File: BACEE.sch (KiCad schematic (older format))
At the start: 13 parts, among them U1 DS1337_PDv2, U2 24LC1025, U3 24LC1025, U4 ATMEGA328P-AU, Y1 Crystal, Y2 Crystal

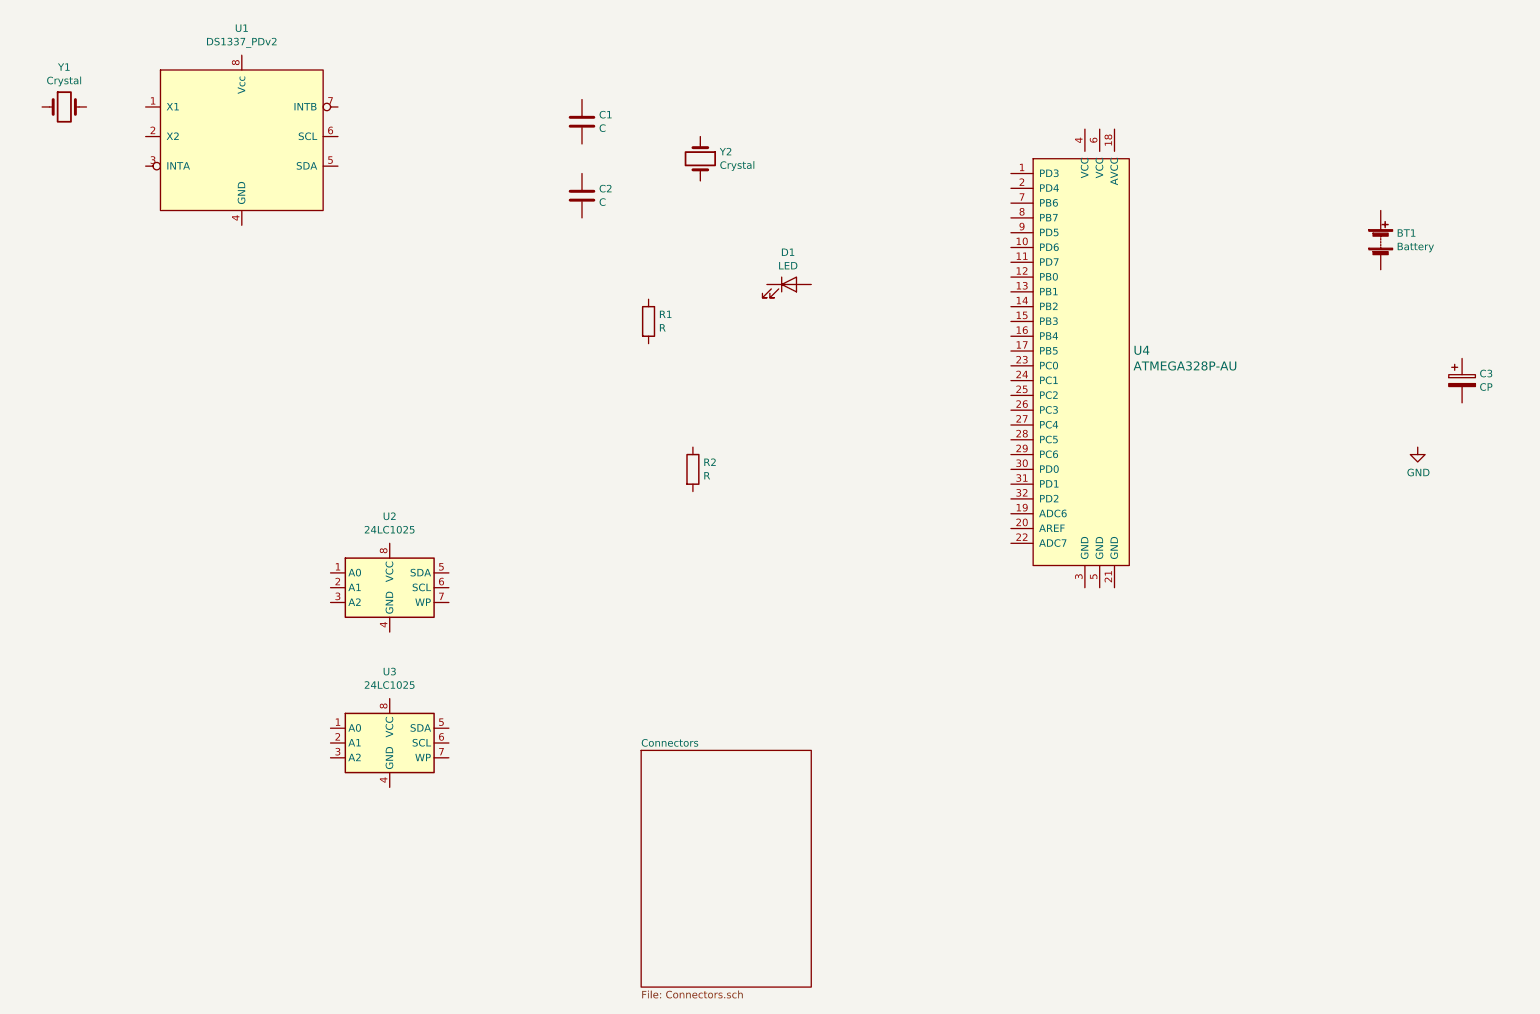
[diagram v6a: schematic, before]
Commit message: Completed wiring in connector sheet
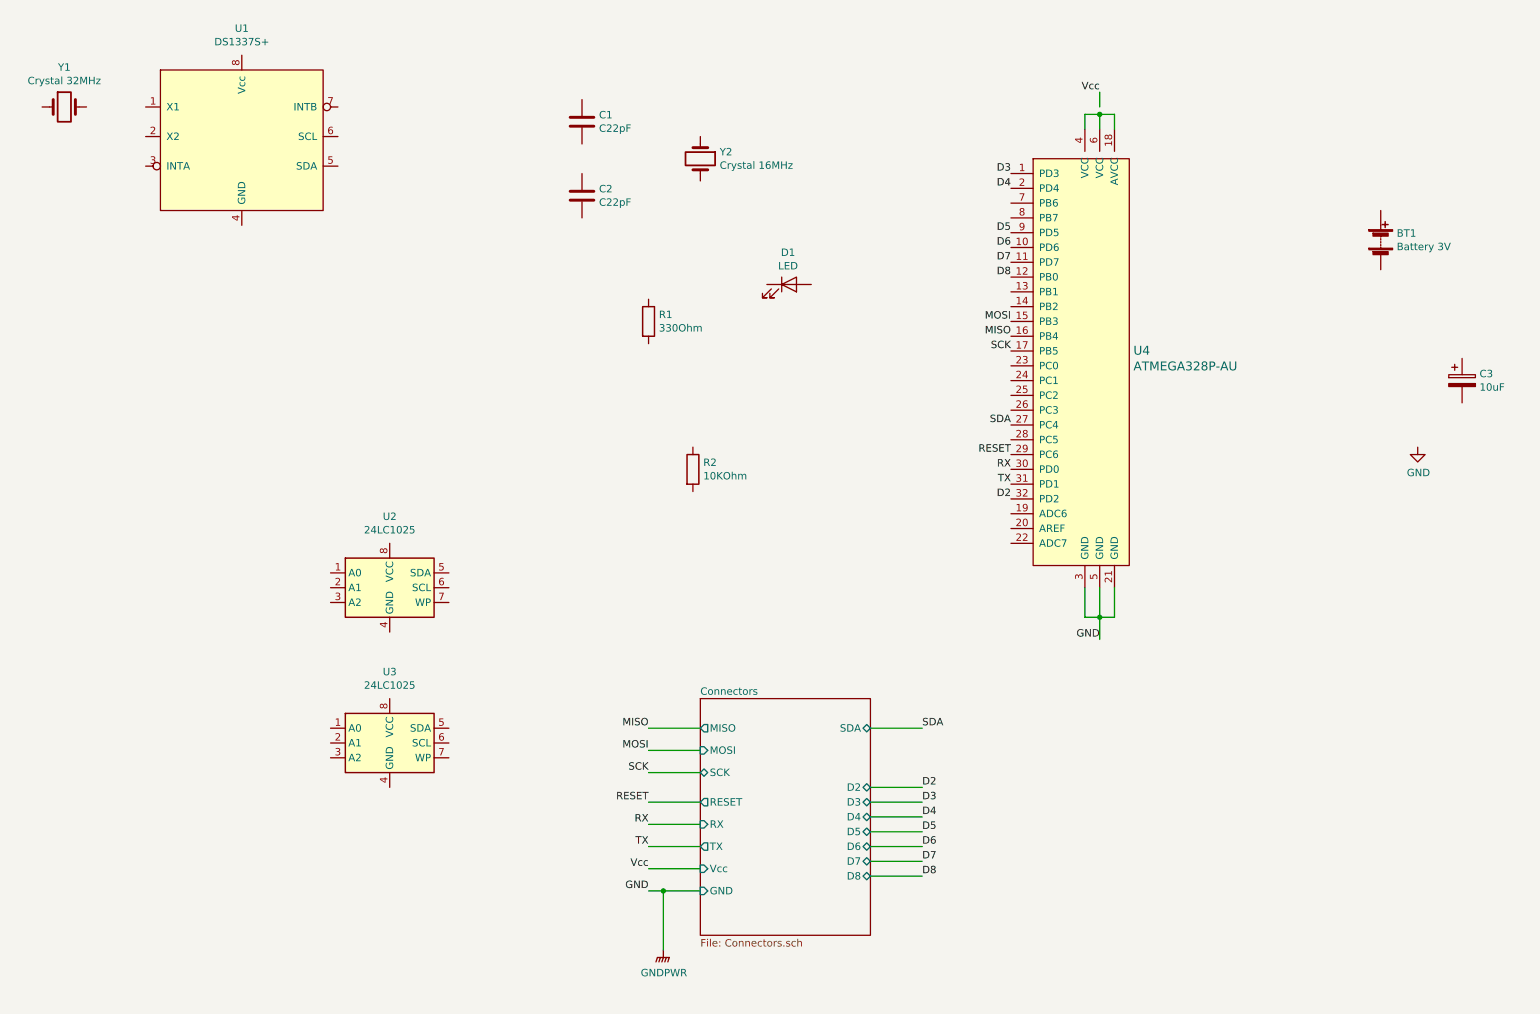
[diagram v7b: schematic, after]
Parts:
- BT1: value Battery -> Battery 3V
- C1, C2: value C -> C22pF
- C3: value CP -> 10uF
- R1: value R -> 330Ohm
- R2: value R -> 10KOhm
- U1: value DS1337_PDv2 -> DS1337S+
- Y1: value Crystal -> Crystal 32MHz
- Y2: value Crystal -> Crystal 16MHz
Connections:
- net labels added: D2, D3, D4, D5, D6, D7, D8, GNDPWR, MISO, MOSI, RESET, RX, SCK, SDA, TX, Vcc
- wire segments 0 -> 30
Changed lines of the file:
@@
 P 9800 2600
 F 0 "BT1" H 9908 2646 50  0000 L CNN
-F 1 "Battery" H 9908 2555 50  0000 L CNN
+F 1 "Battery 3V" H 9908 2555 50  0000 L CNN
 F 2 "Connector_PinHeader_2.54mm:PinHeader_1x02_P2.54mm_Vertical" V 9800 2660 50  0001 C CNN
 F 3 "~" V 9800 2660 50  0001 C CNN
@@
 P 4400 1800
 F 0 "C1" H 4515 1846 50  0000 L CNN
-F 1 "C" H 4515 1755 50  0000 L CNN
+F 1 "C22pF" H 4515 1755 50  0000 L CNN
 F 2 "Capacitor_SMD:C_0805_2012Metric_Pad1.15x1.40mm_HandSolder" H 4438 1650 50  0001 C CNN
 F 3 "~" H 4400 1800 50  0001 C CNN
@@
 P 4400 2300
 F 0 "C2" H 4515 2346 50  0000 L CNN
-F 1 "C" H 4515 2255 50  0000 L CNN
+F 1 "C22pF" H 4515 2255 50  0000 L CNN
 F 2 "Capacitor_SMD:C_0805_2012Metric_Pad1.15x1.40mm_HandSolder" H 4438 2150 50  0001 C CNN
 F 3 "~" H 4400 2300 50  0001 C CNN
@@
 P 10350 3550
 F 0 "C3" H 10468 3596 50  0000 L CNN
-F 1 "CP" H 10468 3505 50  0000 L CNN
+F 1 "10uF" H 10468 3505 50  0000 L CNN
 F 2 "Capacitor_SMD:C_0805_2012Metric_Pad1.15x1.40mm_HandSolder" H 10388 3400 50  0001 C CNN
 F 3 "~" H 10350 3550 50  0001 C CNN
@@
 P 4850 3150
 F 0 "R1" H 4920 3196 50  0000 L CNN
-F 1 "R" H 4920 3105 50  0000 L CNN
+F 1 "330Ohm" H 4920 3105 50  0000 L CNN
 F 2 "Resistor_SMD:R_0805_2012Metric_Pad1.15x1.40mm_HandSolder" V 4780 3150 50  0001 C CNN
 F 3 "~" H 4850 3150 50  0001 C CNN
@@
 P 5150 4150
 F 0 "R2" H 5220 4196 50  0000 L CNN
-F 1 "R" H 5220 4105 50  0000 L CNN
+F 1 "10KOhm" H 5220 4105 50  0000 L CNN
 F 2 "Resistor_SMD:R_0805_2012Metric_Pad1.15x1.40mm_HandSolder" V 5080 4150 50  0001 C CNN
 F 3 "~" H 5150 4150 50  0001 C CNN
@@
 $EndComp
 $Sheet
-S 4800 6050 1150 1600
+S 5200 5700 1150 1600
 U 5EC178C4
 F0 "Connectors" 50
 F1 "Connectors.sch" 50
+F2 "MISO" O L 5200 5900 50
+F3 "SCK" B L 5200 6200 50
+F4 "RESET" O L 5200 6400 50
+F5 "Vcc" I L 5200 6850 50
+F6 "MOSI" I L 5200 6050 50
+F7 "GND" I L 5200 7000 50
+F8 "RX" I L 5200 6550 50
+F9 "TX" O L 5200 6700 50
+F10 "SDA" B R 6350 5900 50
+F11 "D2" B R 6350 6300 50
+F12 "D3" B R 6350 6400 50
+F13 "D4" B R 6350 6500 50
+F14 "D5" B R 6350 6600 50
+F15 "D6" B R 6350 6700 50
+F16 "D8" B R 6350 6900 50
+F17 "D7" B R 6350 6800 50
 $EndSheet
 $Comp
@@
 P 2100 1900
 F 0 "U1" H 2100 2631 50  0000 C CNN
-F 1 "DS1337_PDv2" H 2100 2540 50  0000 C CNN
+F 1 "DS1337S+" H 2100 2540 50  0000 C CNN
 F 2 "Package_SO:SOIJ-8_5.3x5.3mm_P1.27mm" H 3050 2400 50  0001 C CNN
 F 3 "https://4donline.ihs.com/images/VipMasterIC/IC/MAXM/MAXM-S-A0000633411/MAXM-S-A0000771822-1.pdf?hkey=52A5661711E402568146F3353EA87419" H 3050 2400 50  0001 C CNN
@@
 P 900 1700
 F 0 "Y1" H 900 1968 50  0000 C CNN
-F 1 "Crystal" H 900 1877 50  0000 C CNN
+F 1 "Crystal 32MHz" H 900 1877 50  0000 C CNN
 F 2 "Crystal:Crystal_SMD_MicroCrystal_CC7V-T1A-2Pin_3.2x1.5mm" H 900 1700 50  0001 C CNN
 F 3 "~" H 900 1700 50  0001 C CNN
@@
 P 5200 2050
 F 0 "Y2" V 5154 2181 50  0000 L CNN
-F 1 "Crystal" V 5245 2181 50  0000 L CNN
+F 1 "Crystal 16MHz" V 5245 2181 50  0000 L CNN
 F 2 "Crystal:Crystal_SMD_5032-2Pin_5.0x3.2mm_HandSoldering" H 5200 2050 50  0001 C CNN
 F 3 "~" H 5200 2050 50  0001 C CNN
@@
 	1    0    0    -1
 $EndComp
+Text Label 4850 5900 2    50   ~ 0
+MISO
+Wire Wire Line
+	4850 5900 5200 5900
+Text Label 7300 3250 2    50   ~ 0
+MISO
+Text Label 4850 6200 2    50   ~ 0
+SCK
+Text Label 4850 6400 2    50   ~ 0
+RESET
+Text Label 4850 6850 2    50   ~ 0
+Vcc
+Text Label 4850 6050 2    50   ~ 0
+MOSI
+Text Label 4850 7000 2    50   ~ 0
+GND
+Wire Wire Line
+	5200 6200 4850 6200
+Wire Wire Line
+	5200 6400 4850 6400
+Wire Wire Line
+	5200 6850 4850 6850
+Wire Wire Line
+	5200 6050 4850 6050
+Wire Wire Line
+	5200 7000 4950 7000
+Text Label 7300 3150 2    50   ~ 0
+MOSI
+Text Label 7300 3350 2    50   ~ 0
+SCK
+Text Label 7300 4050 2    50   ~ 0
+RESET
+Text Label 7900 1600 2    50   ~ 0
+Vcc
+Wire Wire Line
+	7800 1850 7800 1750
+Wire Wire Line
+	7800 1750 7900 1750
+Wire Wire Line
+	8000 1750 8000 1850
+Wire Wire Line
+	7900 1850 7900 1750
+Connection ~ 7900 1750
+Wire Wire Line
+	7900 1750 8000 1750
+Wire Wire Line
+	7900 1700 7900 1600
+Text Label 7900 5300 2    50   ~ 0
+GND
+Wire Wire Line
+	8000 5150 8000 4950
+Wire Wire Line
+	7900 4950 7900 5150
+Wire Wire Line
+	7900 5150 8000 5150
+Wire Wire Line
+	7800 5150 7900 5150
+Connection ~ 7900 5150
+Wire Wire Line
+	7800 4950 7800 5150
+Wire Wire Line
+	7900 5150 7900 5300
+$Comp
+L power:GNDPWR #PWR?
+U 1 1 5EC52C1A
+P 4950 7400
+F 0 "#PWR?" H 4950 7200 50  0001 C CNN
+F 1 "GNDPWR" H 4954 7246 50  0000 C CNN
+F 2 "" H 4950 7350 50  0001 C CNN
+F 3 "" H 4950 7350 50  0001 C CNN
+	1    4950 7400
+	1    0    0    -1
+$EndComp
+Wire Wire Line
+	4950 7400 4950 7000
+Connection ~ 4950 7000
+Wire Wire Line
+	4950 7000 4850 7000
+Text Label 6700 5900 0    50   ~ 0
+SDA
+Text Label 6700 6300 0    50   ~ 0
+D2
+Text Label 6700 6400 0    50   ~ 0
+D3
+Text Label 6700 6500 0    50   ~ 0
+D4
+Text Label 6700 6600 0    50   ~ 0
+D5
+Text Label 6700 6700 0    50   ~ 0
+D6
+Text Label 6700 6800 0    50   ~ 0
+D7
+Text Label 6700 6900 0    50   ~ 0
+D8
+Text Label 4850 6550 2    50   ~ 0
+RX
+Text Label 4850 6700 2    50   ~ 0
+TX
+Wire Wire Line
+	6350 5900 6700 5900
+Wire Wire Line
+	6350 6300 6700 6300
+Wire Wire Line
+	6700 6400 6350 6400
+Wire Wire Line
+	6350 6500 6700 6500
+Wire Wire Line
+	6700 6600 6350 6600
+Wire Wire Line
+	6350 6700 6700 6700
+Wire Wire Line
+	6700 6800 6350 6800
+Wire Wire Line
+	6350 6900 6700 6900
+Wire Wire Line
+	5200 6700 4850 6700
+Wire Wire Line
+	5200 6550 4850 6550
+Text Label 7300 2150 2    50   ~ 0
+D3
+Text Label 7300 2250 2    50   ~ 0
+D4
+Text Label 7300 2550 2    50   ~ 0
+D5
+Text Label 7300 2650 2    50   ~ 0
+D6
+Text Label 7300 2750 2    50   ~ 0
+D7
+Text Label 7300 2850 2    50   ~ 0
+D8
+Text Label 7300 3850 2    50   ~ 0
+SDA
+Text Label 7300 4150 2    50   ~ 0
+RX
+Text Label 7300 4250 2    50   ~ 0
+TX
+Text Label 7300 4350 2    50   ~ 0
+D2
 $EndSCHEMATC

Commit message: Completed wiring in root sheet
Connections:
- net labels added: ADDS1, ADDS2
- wire segments 30 -> 95
- no-connect marks 0 -> 13
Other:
- moved on the sheet: BT1, C1, C2, C3, D1, R1, R2, U2, U3, Y1, Y2
